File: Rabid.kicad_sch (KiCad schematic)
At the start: 215 parts, among them J1 USB Header, SW1 Key, SW10 Key, SW100 Key, SW101 Key, SW102 Key, SW11 Key, SW12 Key, SW13 Key, SW14 Key, SW15 Key, SW16 Key, SW17 Key, SW18 Key, SW19 Key, SW2 Key, SW20 Key, SW21 Key, SW22 Key, SW23 Key, SW24 Key, SW25 Key, SW26 Key, SW27 Key, SW28 Key, SW29 Key, SW3 Key, SW30 Key, SW31 Key, SW32 Key, SW33 Key, SW34 Key, SW35 Key, SW36 Key, SW37 Key, SW38 Key, SW39 Key, SW4 Key, SW40 Key, SW41 Key, SW42 Key, SW43 Key, SW44 Key, SW45 Key, SW46 Key, SW47 Key, SW48 Key, SW49 Key, SW5 Key, SW50 Key, SW51 Key, SW52 Key, SW53 Key, SW54 Key, SW55 Key, SW56 Key, SW57 Key, SW58 Key, SW59 Key, SW6 Key, SW60 Key, SW61 Key, SW62 Key, SW63 Key, SW64 Key, SW65 Key, SW66 Key, SW67 Key, SW68 Key, SW69 Key, SW7 Key, SW70 Key, SW71 Key, SW72 Key, SW73 Key, SW74 Key, SW75 Key, SW76 Key, SW77 Key, SW78 Key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

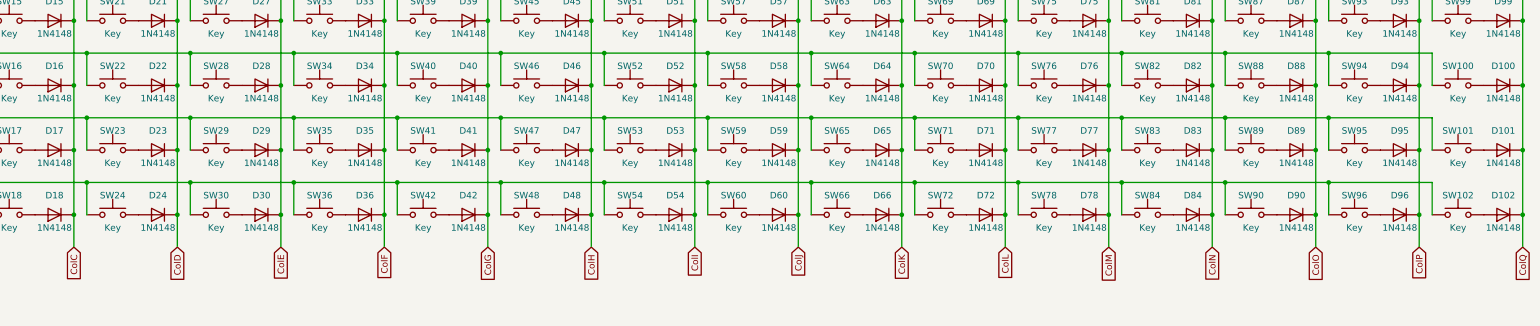
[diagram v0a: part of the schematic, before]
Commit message: Everything in its approximate location.
TODO:
 - Still needs comparison to a real PCB to get measurements more accurate.
 - Needs mounting holes.
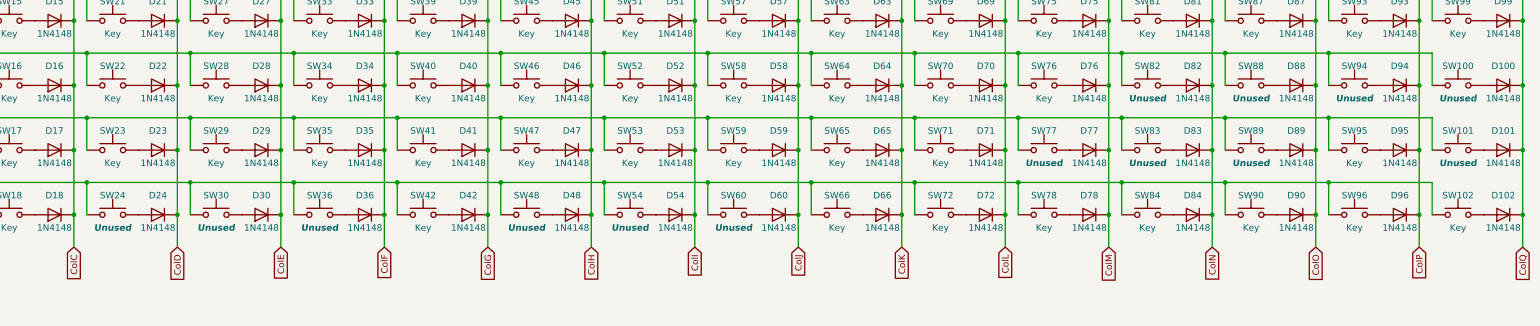
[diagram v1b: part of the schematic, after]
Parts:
- D100, D101, D24, D30, D36, D48, D54, D60, D7, D77, D82, D83, D88, D89, D94, SW7: now left out of the parts list
- SW100, SW101, SW24, SW30, SW36, SW48, SW54, SW60, SW77, SW82, SW83, SW88, SW89, SW94: value Key -> Unused; now left out of the parts list
- SW12, SW18, SW6, SW66, SW72, SW78, SW84: footprint Button_Switch_Keyboard:SW_Cherry_MX_1.00u_PCB -> Button_Switch_Keyboard:SW_Cherry_MX_1.25u_PCB
- SW3, SW81: footprint Button_Switch_Keyboard:SW_Cherry_MX_1.00u_PCB -> Button_Switch_Keyboard:SW_Cherry_MX_1.50u_PCB
- SW4: footprint Button_Switch_Keyboard:SW_Cherry_MX_1.00u_PCB -> Button_Switch_Keyboard:SW_Cherry_MX_1.75u_PCB
- SW42: footprint Button_Switch_Keyboard:SW_Cherry_MX_1.00u_PCB -> Button_Switch_Keyboard:SW_Cherry_MX_6.25u_PCB
- SW5, SW76: footprint Button_Switch_Keyboard:SW_Cherry_MX_1.00u_PCB -> Button_Switch_Keyboard:SW_Cherry_MX_2.25u_PCB
- SW71: footprint Button_Switch_Keyboard:SW_Cherry_MX_1.00u_PCB -> Button_Switch_Keyboard:SW_Cherry_MX_2.75u_PCB
- SW80: footprint Button_Switch_Keyboard:SW_Cherry_MX_1.00u_PCB -> Button_Switch_Keyboard:SW_Cherry_MX_2.00u_PCB

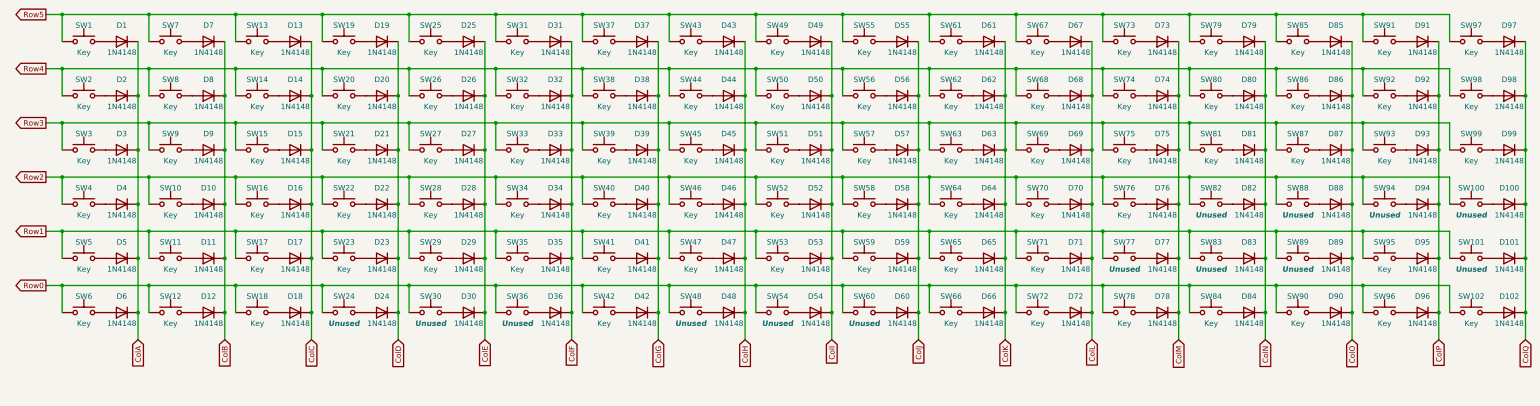
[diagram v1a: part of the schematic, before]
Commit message: Name the keys on F.Fab layer.
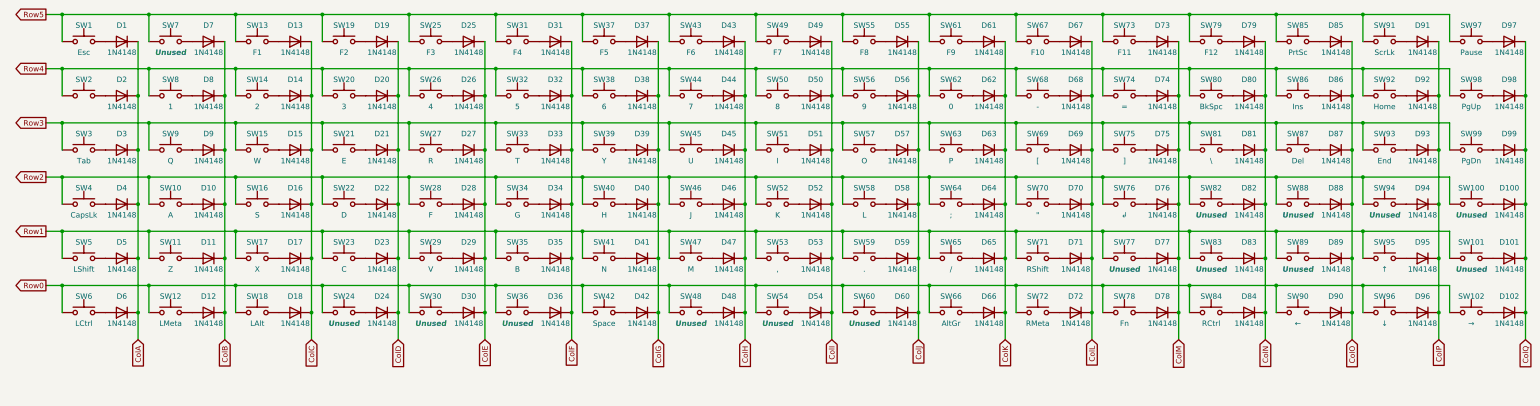
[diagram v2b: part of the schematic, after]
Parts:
- SW1: value Key -> Esc
- SW10: value Key -> A
- SW102: value Key -> →
- SW11: value Key -> Z
- SW12: value Key -> LMeta
- SW13: value Key -> F1
- SW14: value Key -> 2
- SW15: value Key -> W
- SW16: value Key -> S
- SW17: value Key -> X
- SW18: value Key -> LAlt
- SW19: value Key -> F2
- SW2: value Key -> ~
- SW20: value Key -> 3
- SW21: value Key -> E
- SW22: value Key -> D
- SW23: value Key -> C
- SW25: value Key -> F3
- SW26: value Key -> 4
- SW27: value Key -> R
- SW28: value Key -> F
- SW29: value Key -> V
- SW3: value Key -> Tab
- SW31: value Key -> F4
- SW32: value Key -> 5
- SW33: value Key -> T
- SW34: value Key -> G
- SW35: value Key -> B
- SW37: value Key -> F5
- SW38: value Key -> 6
- SW39: value Key -> Y
- SW4: value Key -> CapsLk
- SW40: value Key -> H
- SW41: value Key -> N
- SW42: value Key -> Space
- SW43: value Key -> F6
- SW44: value Key -> 7
- SW45: value Key -> U
- SW46: value Key -> J
- SW47: value Key -> M
- SW49: value Key -> F7
- SW5: value Key -> LShift
- SW50: value Key -> 8
- SW51: value Key -> I
- SW52: value Key -> K
- SW53: value Key -> ,
- SW55: value Key -> F8
- SW56: value Key -> 9
- SW57: value Key -> O
- SW58: value Key -> L
- SW59: value Key -> .
- SW6: value Key -> LCtrl
- SW61: value Key -> F9
- SW62: value Key -> 0
- SW63: value Key -> P
- SW64: value Key -> ;
- SW65: value Key -> /
- SW66: value Key -> AltGr
- SW67: value Key -> F10
- SW68: value Key -> -
- SW69: value Key -> [
- SW7: value Key -> Unused
- SW70: value Key -> "
- SW71: value Key -> RShift
- SW72: value Key -> RMeta
- SW73: value Key -> F11
- SW74: value Key -> =
- SW75: value Key -> ]
- SW76: value Key -> ↲
- SW78: value Key -> Fn
- SW79: value Key -> F12
- SW8: value Key -> 1
- SW80: value Key -> BkSpc
- SW81: value Key -> \
- SW84: value Key -> RCtrl
- SW85: value Key -> PrtSc
- SW86: value Key -> Ins
- SW87: value Key -> Del
- SW9: value Key -> Q
- SW90: value Key -> ←
- SW91: value Key -> ScrLk
- SW92: value Key -> Home
- SW93: value Key -> End
- SW95: value Key -> ↑
- SW96: value Key -> ↓
- SW97: value Key -> Pause
- SW98: value Key -> PgUp
- SW99: value Key -> PgDn

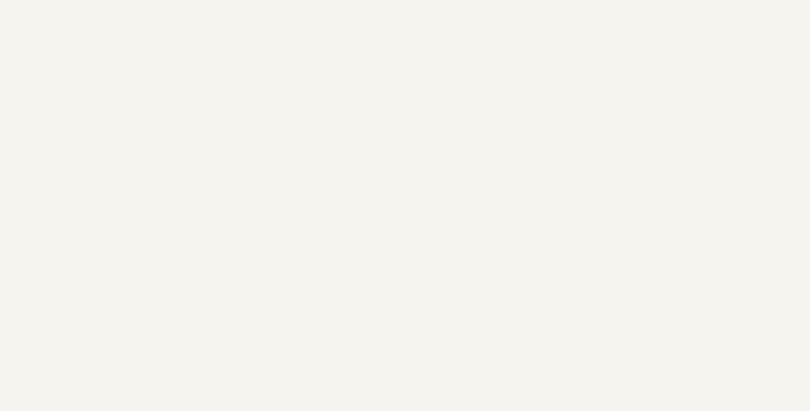
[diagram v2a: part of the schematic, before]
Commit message: Add mounting holes.
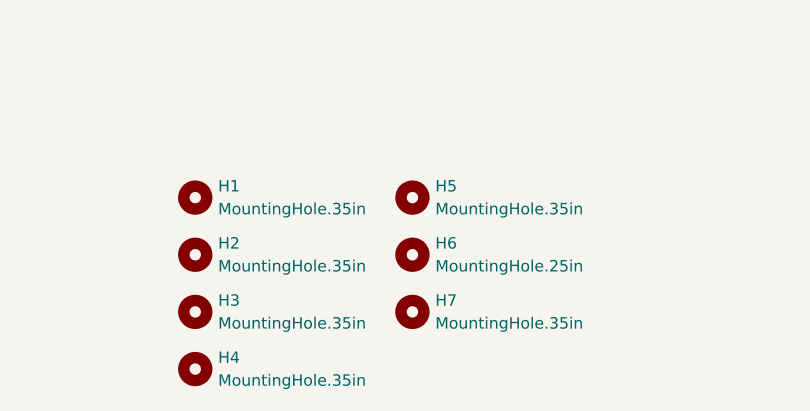
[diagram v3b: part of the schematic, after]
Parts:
- added H1, H2, H3, H4, H5, H7: MountingHole.35in, MountingHole:MountingHole_4.3mm_M4, symbol Mechanical:MountingHole
- added H6: MountingHole.25in, MountingHole:MountingHole_4.3mm_M4, symbol Mechanical:MountingHole
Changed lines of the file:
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@@
     (pin "2")
   )
+  (symbol (lib_id "Mechanical:MountingHole") (at 278.13 274.32 0) (unit 1)
+    (in_bom yes) (on_board yes) (fields_autoplaced)
+    (property "Reference" "H7" (id 0) (at 280.67 273.0499 0)
+      (effects (font (size 1.27 1.27)) (justify left))
+    )
+    (property "Value" "MountingHole.35in" (id 1) (at 280.67 275.5899 0)
+      (effects (font (size 1.27 1.27)) (justify left))
+    )
+    (property "Footprint" "MountingHole:MountingHole_4.3mm_M4" (id 2) (at 278.13 274.32 0)
+      (effects (font (size 1.27 1.27)) hide)
+    )
+    (property "Datasheet" "~" (id 3) (at 278.13 274.32 0)
+      (effects (font (size 1.27 1.27)) hide)
+    )
+  )
   (symbol (lib_id "Diode:1N4148") (at 260.35 80.01 180) (unit 1)
     (in_bom yes) (on_board yes)
@@
     (pin "2")
   )
+  (symbol (lib_id "Mechanical:MountingHole") (at 254 274.32 0) (unit 1)
+    (in_bom yes) (on_board yes) (fields_autoplaced)
+    (property "Reference" "H3" (id 0) (at 256.54 273.0499 0)
+      (effects (font (size 1.27 1.27)) (justify left))
+    )
+    (property "Value" "MountingHole.35in" (id 1) (at 256.54 275.5899 0)
+      (effects (font (size 1.27 1.27)) (justify left))
+    )
+    (property "Footprint" "MountingHole:MountingHole_4.3mm_M4" (id 2) (at 254 274.32 0)
+      (effects (font (size 1.27 1.27)) hide)
+    )
+    (property "Datasheet" "~" (id 3) (at 254 274.32 0)
+      (effects (font (size 1.27 1.27)) hide)
+    )
+  )
   (symbol (lib_id "rp2040_stamp:RP2040_Stamp") (at 92.71 215.9 90) (unit 1)
     (in_bom yes) (on_board yes) (fields_autoplaced)
@@
     (pin "2")
   )
+  (symbol (lib_id "Mechanical:MountingHole") (at 254 280.67 0) (unit 1)
+    (in_bom yes) (on_board yes) (fields_autoplaced)
+    (property "Reference" "H4" (id 0) (at 256.54 279.3999 0)
+      (effects (font (size 1.27 1.27)) (justify left))
+    )
+    (property "Value" "MountingHole.35in" (id 1) (at 256.54 281.9399 0)
+      (effects (font (size 1.27 1.27)) (justify left))
+    )
+    (property "Footprint" "MountingHole:MountingHole_4.3mm_M4" (id 2) (at 254 280.67 0)
+      (effects (font (size 1.27 1.27)) hide)
+    )
+    (property "Datasheet" "~" (id 3) (at 254 280.67 0)
+      (effects (font (size 1.27 1.27)) hide)
+    )
+  )
   (symbol (lib_id "Diode:1N4148") (at 361.95 67.31 180) (unit 1)
     (in_bom no) (on_board no)
@@
     (pin "2")
   )
+  (symbol (lib_id "Mechanical:MountingHole") (at 278.13 261.62 0) (unit 1)
+    (in_bom yes) (on_board yes) (fields_autoplaced)
+    (property "Reference" "H5" (id 0) (at 280.67 260.3499 0)
+      (effects (font (size 1.27 1.27)) (justify left))
+    )
+    (property "Value" "MountingHole.35in" (id 1) (at 280.67 262.8899 0)
+      (effects (font (size 1.27 1.27)) (justify left))
+    )
+    (property "Footprint" "MountingHole:MountingHole_4.3mm_M4" (id 2) (at 278.13 261.62 0)
+      (effects (font (size 1.27 1.27)) hide)
+    )
+    (property "Datasheet" "~" (id 3) (at 278.13 261.62 0)
+      (effects (font (size 1.27 1.27)) hide)
+    )
+  )
   (symbol (lib_id "Diode:1N4148") (at 158.75 92.71 180) (unit 1)
     (in_bom no) (on_board no)
@@
     (pin "2")
   )
+  (symbol (lib_id "Mechanical:MountingHole") (at 254 261.62 0) (unit 1)
+    (in_bom yes) (on_board yes) (fields_autoplaced)
+    (property "Reference" "H1" (id 0) (at 256.54 260.3499 0)
+      (effects (font (size 1.27 1.27)) (justify left))
+    )
+    (property "Value" "MountingHole.35in" (id 1) (at 256.54 262.8899 0)
+      (effects (font (size 1.27 1.27)) (justify left))
+    )
+    (property "Footprint" "MountingHole:MountingHole_4.3mm_M4" (id 2) (at 254 261.62 0)
+      (effects (font (size 1.27 1.27)) hide)
+    )
+    (property "Datasheet" "~" (id 3) (at 254 261.62 0)
+      (effects (font (size 1.27 1.27)) hide)
+    )
+  )
   (symbol (lib_id "Switch:SW_Push") (at 353.06 80.01 0) (unit 1)
     (in_bom yes) (on_board yes)
@@
     (pin "2")
   )
+  (symbol (lib_id "Mechanical:MountingHole") (at 254 267.97 0) (unit 1)
+    (in_bom yes) (on_board yes) (fields_autoplaced)
+    (property "Reference" "H2" (id 0) (at 256.54 266.6999 0)
+      (effects (font (size 1.27 1.27)) (justify left))
+    )
+    (property "Value" "MountingHole.35in" (id 1) (at 256.54 269.2399 0)
+      (effects (font (size 1.27 1.27)) (justify left))
+    )
+    (property "Footprint" "MountingHole:MountingHole_4.3mm_M4" (id 2) (at 254 267.97 0)
+      (effects (font (size 1.27 1.27)) hide)
+    )
+    (property "Datasheet" "~" (id 3) (at 254 267.97 0)
+      (effects (font (size 1.27 1.27)) hide)
+    )
+  )
   (symbol (lib_id "Switch:SW_Push") (at 312.42 92.71 0) (unit 1)
     (in_bom yes) (on_board yes)
@@
     (pin "2")
   )
+  (symbol (lib_id "Mechanical:MountingHole") (at 278.13 267.97 0) (unit 1)
+    (in_bom yes) (on_board yes)
+    (property "Reference" "H6" (id 0) (at 280.67 266.6999 0)
+      (effects (font (size 1.27 1.27)) (justify left))
+    )
+    (property "Value" "MountingHole.25in" (id 1) (at 280.67 269.2399 0)
+      (effects (font (size 1.27 1.27)) (justify left))
+    )
+    (property "Footprint" "MountingHole:MountingHole_4.3mm_M4" (id 2) (at 278.13 267.97 0)
+      (effects (font (size 1.27 1.27)) hide)
+    )
+    (property "Datasheet" "~" (id 3) (at 278.13 267.97 0)
+      (effects (font (size 1.27 1.27)) hide)
+    )
+  )
   (symbol (lib_id "Switch:SW_Push") (at 88.9 80.01 0) (unit 1)
     (in_bom yes) (on_board yes)
@@
       (reference "D108") (unit 1) (value "FnTopLED") (footprint "LED_THT:LED_D3.0mm")
     )
+    (path "/7ab71991-2b35-4dfe-a3d1-e1d6a93c8aa2"
+      (reference "H1") (unit 1) (value "MountingHole.35in") (footprint "MountingHole:MountingHole_4.3mm_M4")
+    )
+    (path "/84b27060-4b68-4266-a520-6b17d4002257"
+      (reference "H2") (unit 1) (value "MountingHole.35in") (footprint "MountingHole:MountingHole_4.3mm_M4")
+    )
+    (path "/18a8f0d3-5ac8-4d2b-aaf1-8fd815948e6a"
+      (reference "H3") (unit 1) (value "MountingHole.35in") (footprint "MountingHole:MountingHole_4.3mm_M4")
+    )
+    (path "/23a84009-b94e-4473-821b-756b9ff8be21"
+      (reference "H4") (unit 1) (value "MountingHole.35in") (footprint "MountingHole:MountingHole_4.3mm_M4")
+    )
+    (path "/6a239d85-40cc-4822-a383-2dc31e36eed3"
+      (reference "H5") (unit 1) (value "MountingHole.35in") (footprint "MountingHole:MountingHole_4.3mm_M4")
+    )
+    (path "/b0e52192-3ce8-4daa-8b02-fbc5aef0027e"
+      (reference "H6") (unit 1) (value "MountingHole.25in") (footprint "MountingHole:MountingHole_4.3mm_M4")
+    )
+    (path "/02f4d47d-ab1d-4f2f-9935-90a7fb385495"
+      (reference "H7") (unit 1) (value "MountingHole.35in") (footprint "MountingHole:MountingHole_4.3mm_M4")
+    )
     (path "/bbea82d0-8c64-4c6e-81d8-7d16f5942bd3"

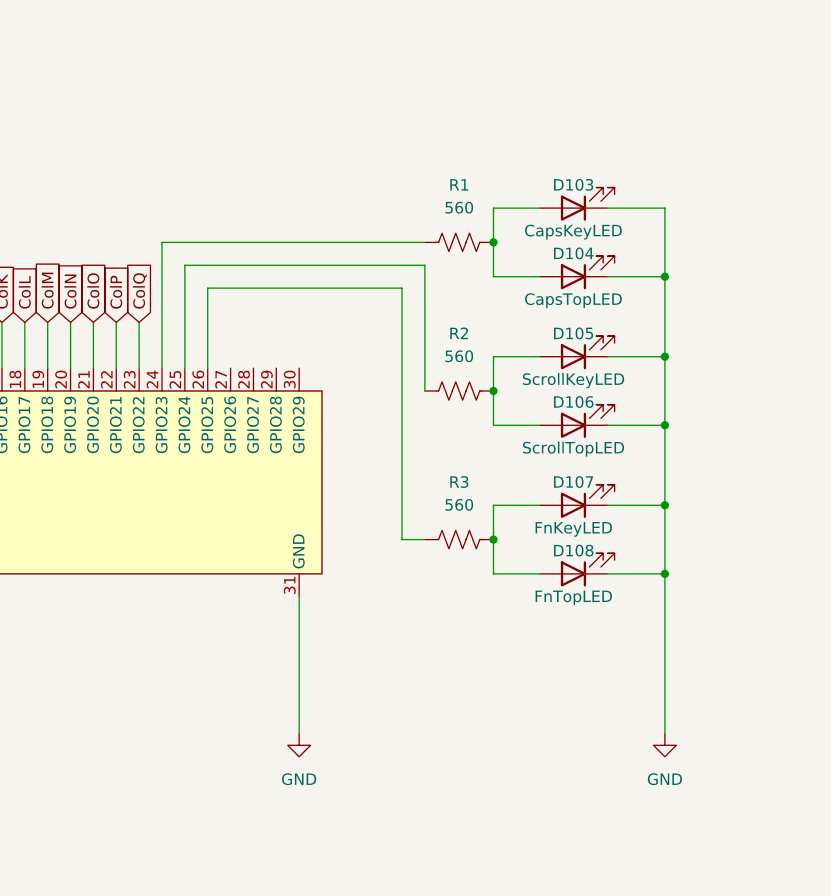
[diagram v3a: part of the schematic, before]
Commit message: LED tracks routed.
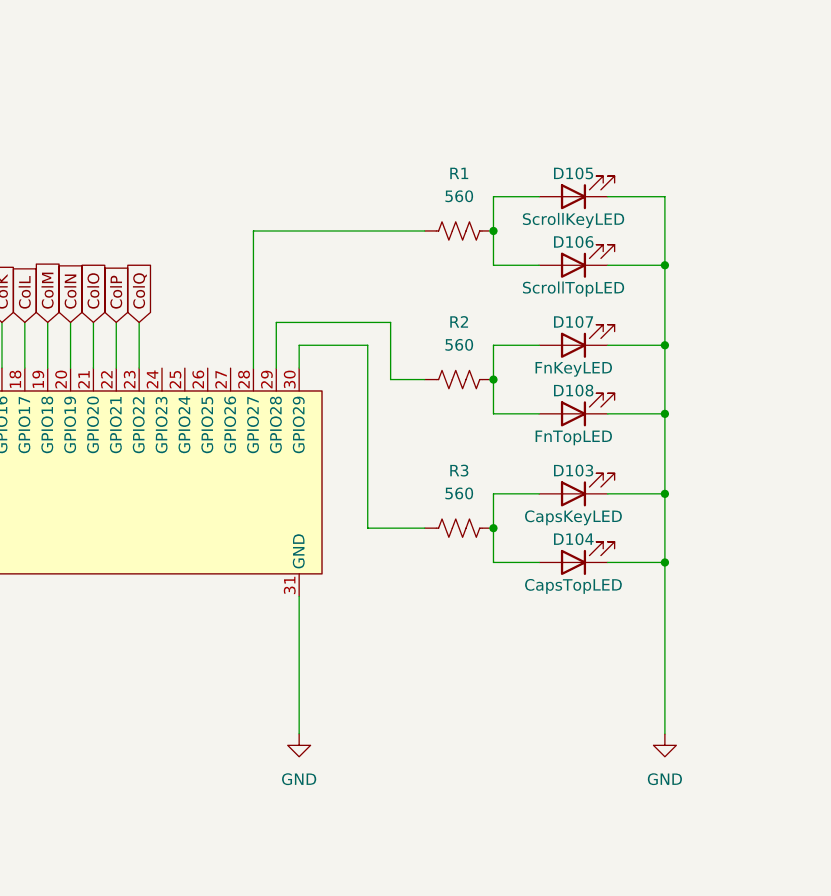
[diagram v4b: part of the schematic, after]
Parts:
- renumbered R2 to R1, R3 to R2, R1 to R3
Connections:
- net at R2.1: now also U1.29 (GPIO28); no longer U1.26 (GPIO25)
- net at U1.24 (GPIO23): no longer R3.1
- net at U1.25 (GPIO24): no longer R1.1
- net at U1.28 (GPIO27): now also R1.1
- net at U1.30 (GPIO29): now also R3.1
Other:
- moved on the sheet: D103, D104, D105, D106, D107, D108, R1, R2, R3
